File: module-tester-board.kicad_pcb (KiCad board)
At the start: 2 copper layers, 101.6 x 53.3 mm, 26 parts, among them J1 Conn_01x08_Male, J2 Barrel_Jack, J4 Tester Points, SW1 SW_DIP_x04, U1 LT8330, U4 MCP2515-EST, U5 ATA6560,1, Y1 20MHz

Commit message: 0.0.11 First version of traces
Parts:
- added REF**: , MountingHole:MountingHole_3.2mm_M3, F.Cu at (123.2, 71.4)
- added REF**: , MountingHole:MountingHole_3.2mm_M3, F.Cu at (182.6, 115.1)
- D1: value D_Schottky -> Schottky
- J1: value Conn_01x08_Male -> (none)
- SW1: value SW_DIP_x04 -> (none)
- U4: value MCP2515-EST -> MCP2515
- moved C1 66.3 mm to (164.3, 72.9)
- moved C2 66.1 mm to (164.6, 78.0)
- moved C3 66.1 mm to (175.0, 78.3)
- moved C4 66.1 mm to (177.0, 72.9)
- moved D1 66.1 mm to (169.7, 69.1)
- moved L1 66.1 mm to (165.1, 69.1)
- moved R2 66.1 mm to (167.1, 78.0)
- moved R3 66.1 mm to (171.2, 78.7)
- moved U1 66.1 mm to (170.9, 74.2)
- moved J1 64.8 mm to (175.5, 100.1)
- moved J4 62.3 mm to (170.2, 105.2)
- moved SW1 59.1 mm to (159.0, 105.2)
- moved U5 42.1 mm to (158.0, 74.2)
- moved R4 42.1 mm to (160.0, 80.8)
- moved R5 42.1 mm to (160.0, 68.1)
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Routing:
- net +12V: track 103.5 -> 54.1 mm, vias 3 -> 0
- net A0: track 62.2 -> 17.4 mm
- net PWM1: track 81.9 -> 39.4 mm, vias 0 -> 1
- net PWM0: track 80.6 -> 39.3 mm, vias 0 -> 1
- net A1: track 60.1 -> 23.9 mm, vias 1 -> 0
- net INT: track 74.5 -> 50.0 mm, vias 2 -> 1
- net RX0: track 74.3 -> 50.6 mm, vias 2 -> 1
- net RX1: track 73.1 -> 51.3 mm, vias 2 -> 1
- net TX1: track 59.6 -> 41.3 mm
- net TX2: track 60.1 -> 42.3 mm
- net +48V: track 38.2 -> 22.9 mm
- net +5V: track 62.2 -> 47.5 mm
- net SS: track 64.1 -> 50.8 mm
- net Net-(U4-Pad1): track 18.2 -> 30.3 mm, vias 2 -> 0
- net TX0: track 51.5 -> 40.6 mm, vias 2 -> 1
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- added copper zone on B.Cu, net GND
- added copper zone on F.Cu, net GND
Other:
- board size 101.6 x 53.3 mm -> 69.1 x 53.3 mm
- board text added: "Module Tester Board Made by Sean Martin For MST URT"
- board text added: "Rev 0.0.11 Rev Date 2018-10-01"

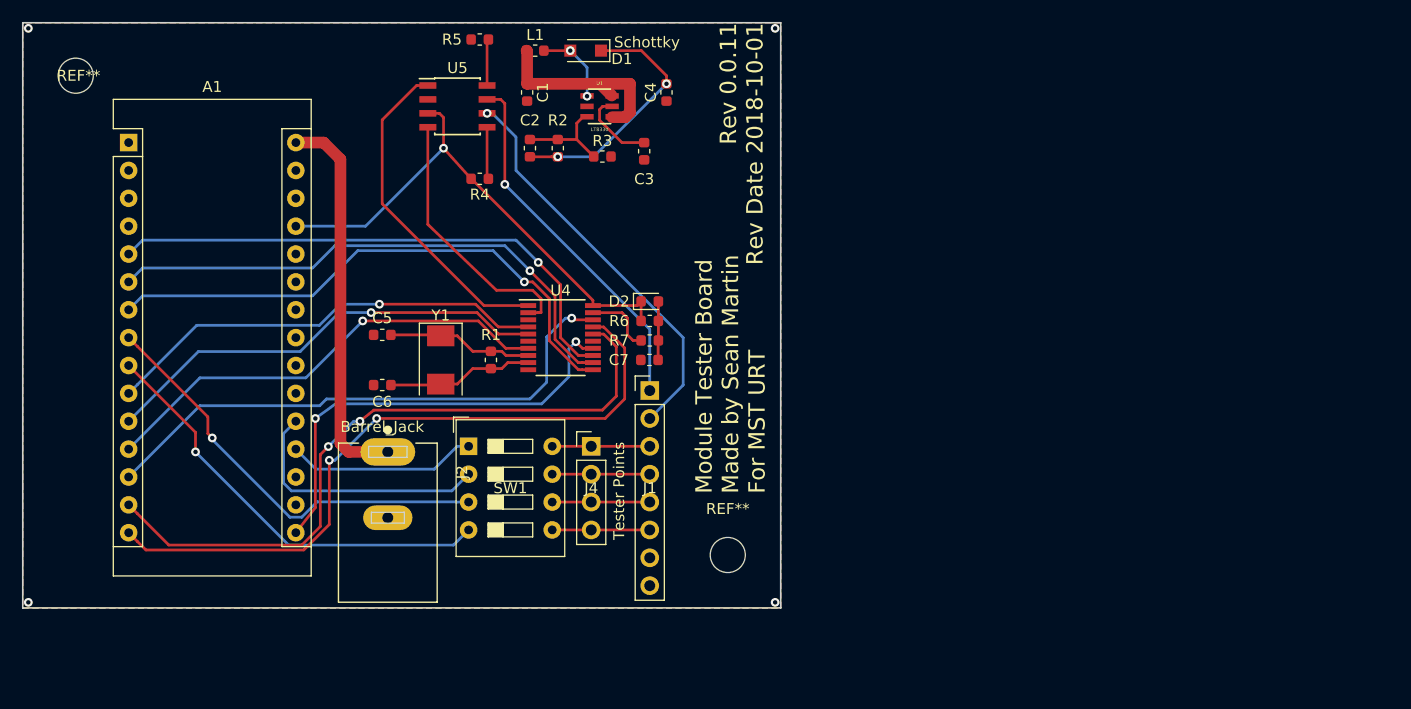
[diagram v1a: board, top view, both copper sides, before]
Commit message: 0.0.12 Fixed board trace and GND plane issues
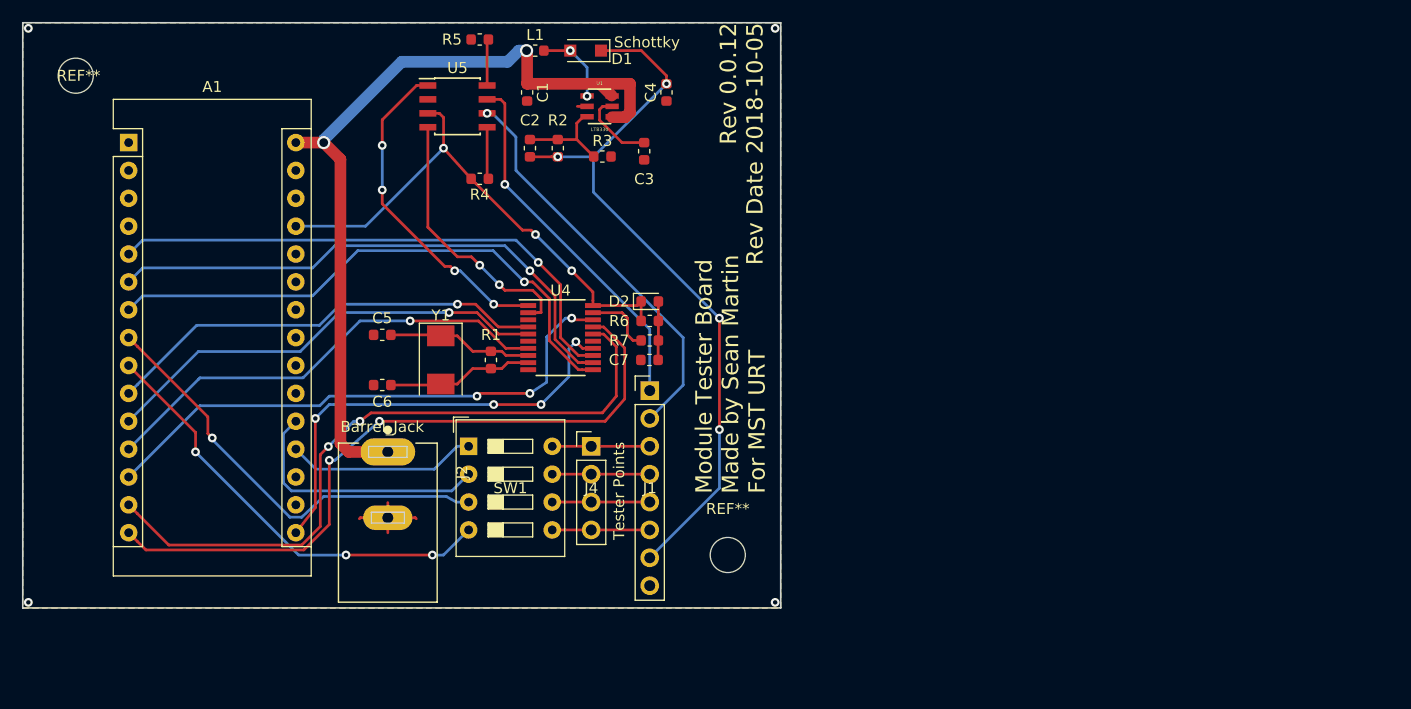
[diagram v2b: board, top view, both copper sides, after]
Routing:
- net +48V: track 22.9 -> 66.8 mm, vias 2 -> 4
- net +12V: track 54.1 -> 76.1 mm, vias 0 -> 2
- net GND: track 0.00 -> 8.91 mm
- net PWM1: track 39.4 -> 40.1 mm, vias 1 -> 3
- net +5V: track 47.5 -> 48.0 mm, vias 1 -> 3
- net Net-(U4-Pad2): track 24.3 -> 24.6 mm, vias 0 -> 2
- net SCK: track 40.8 -> 41.0 mm, vias 2 -> 4
- net SS: track 50.8 -> 50.7 mm, vias 1 -> 3
- net Net-(U4-Pad1): vias 0 -> 4
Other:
- board text added: "Rev 0.0.12 Rev Date 2018-10-05"
- board text removed: "Rev 0.0.11 Rev Date 2018-10-01"
